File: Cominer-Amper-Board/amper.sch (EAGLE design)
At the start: 3 parts, among them U1 ESP-07

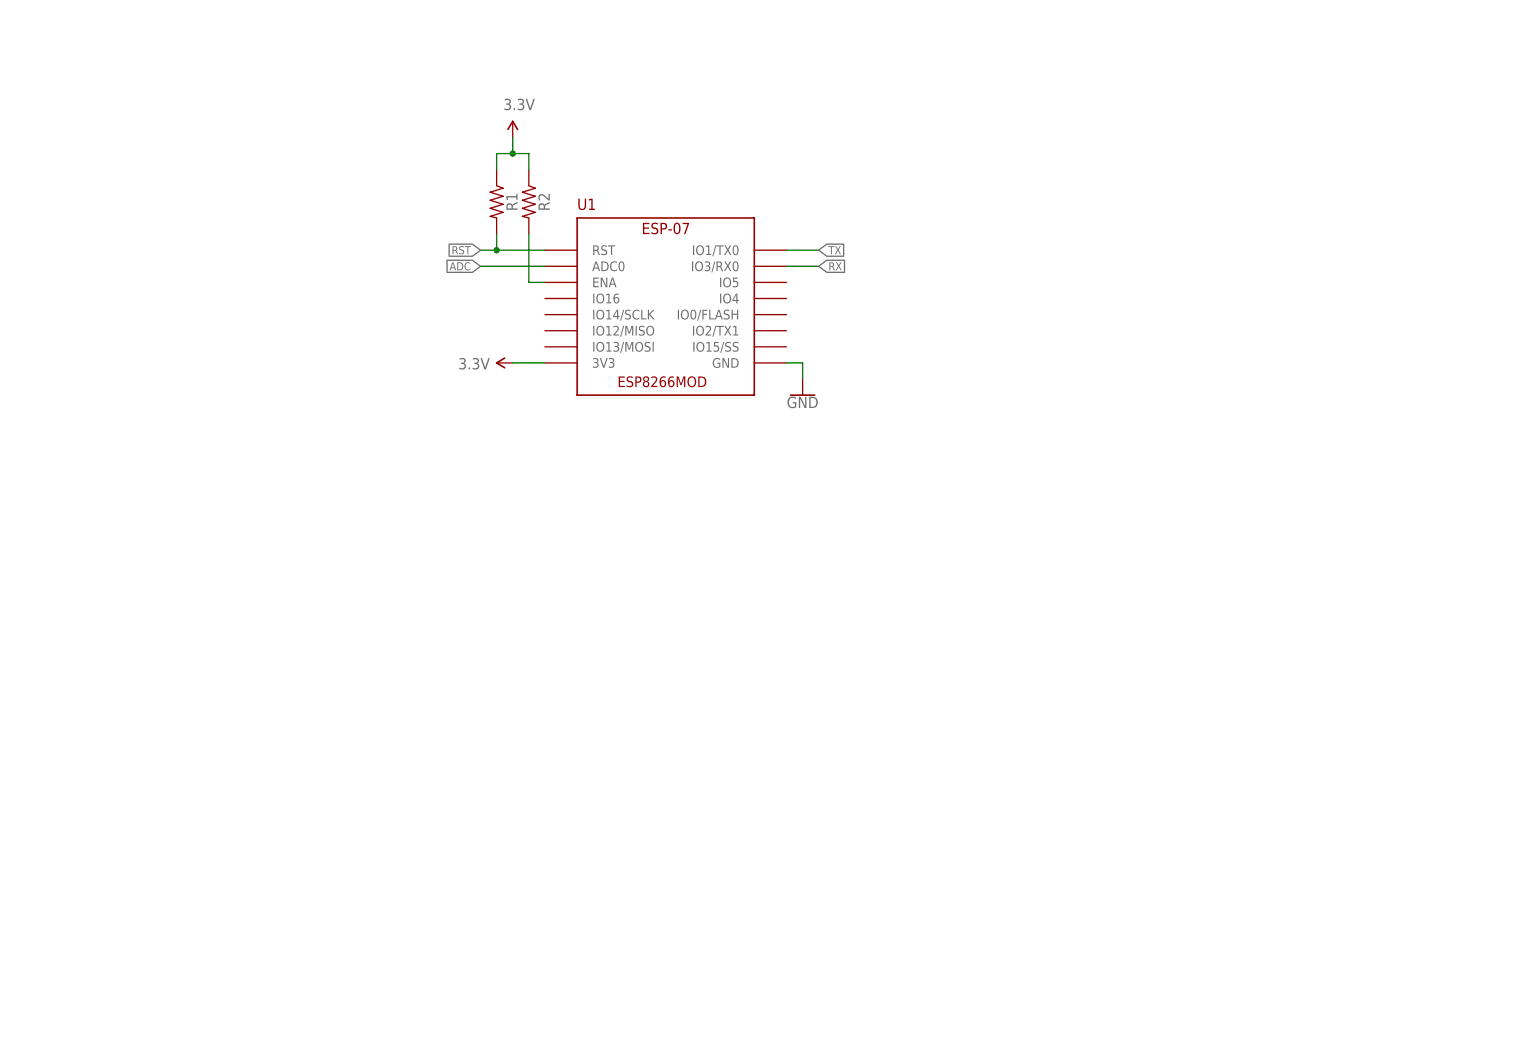
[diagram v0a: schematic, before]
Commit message: add usb to serialport circuit and lm1117 regulator
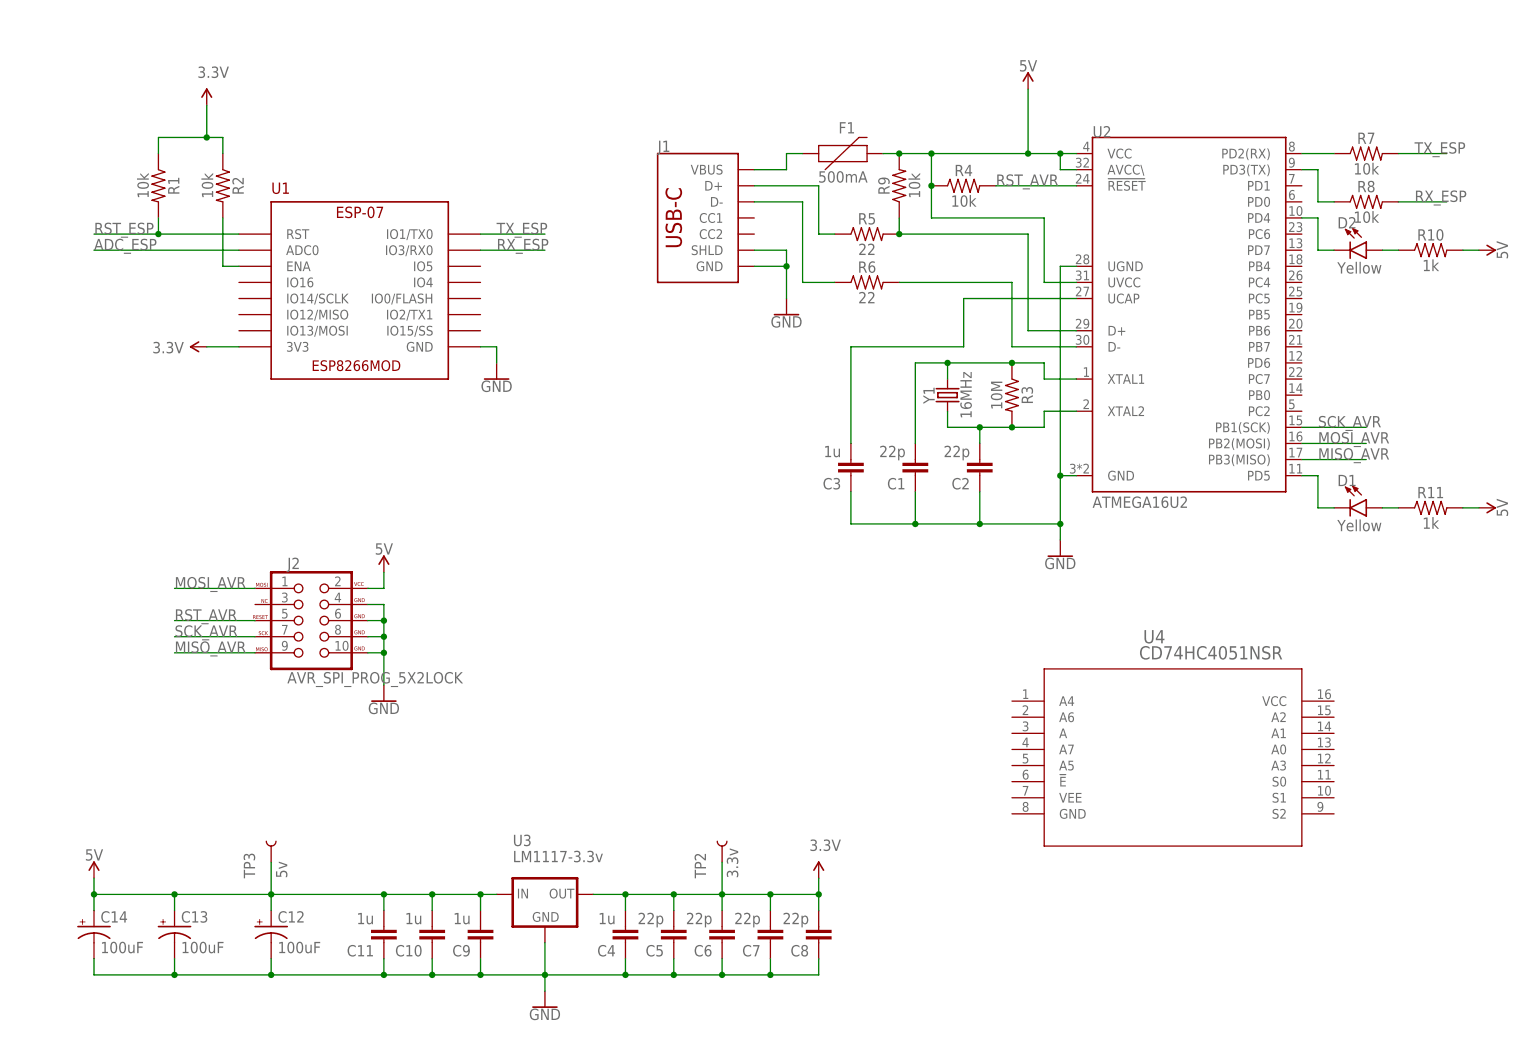
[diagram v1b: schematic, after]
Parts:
- added C1, C2, C5, C6, C7, C8: 22p, SparkFun-Capacitors:CAP-0805
- added C10, C11, C3, C4, C9: 1u, SparkFun-Capacitors:CAP-0805
- added C12, C13, C14: 100uF, SparkFun-Capacitors:100UF-POLAR-25V-20%(ELEC)
- added D1, D2: Yellow, SparkFun-LED:LED-YELLOW0603
- added F1: 500mA, SparkFun-Fuses:PPTC_16V_2.5A
- added J1: (no value), SparkFun-Connectors:USB_C_2-LAYER_PADS
- added J2: AVR_SPI_PROG_5X2LOCK, SparkFun-Connectors:AVR_SPI_PROG_5X2LOCK
- added R10, R11: 1k, SparkFun-Resistors:RESISTOR0805
- added R3: 10M, SparkFun-Resistors:RESISTOR0805
- added R4, R7, R8, R9: 10k, SparkFun-Resistors:RESISTOR0805
- added R5, R6: 22, SparkFun-Resistors:RESISTOR0805
- added TP2: 3.3v, SparkFun-Connectors:TEST-POINT3X4
- added TP3: 5v, SparkFun-Connectors:TEST-POINT3X4
- added U2: ATMEGA16U2, Cominer-Microcontroller:ATMEGA16U2
- added U3: LM1117-3.3v, SparkFun-IC-Power:V_REG_LD1117VXXLD1117-SMD
- added U4: CD74HC4051NSR, Cominer-CD74HC4051NSR:CD74HC4051NSR
- added Y1: 16MHz, SparkFun-Clocks:CRYSTAL-16MHZSMD-5X3.2
- R1, R2: value (none) -> 10k
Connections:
- net ADC renamed ADC_ESP
- net RST renamed RST_ESP
- removed net RX: U1.IO3/RX0
- removed net TX: U1.IO1/TX0
- new net 5V: C10.2, C11.2, C12.+, C13.+, C14.+, C9.2, F1.2, J2.VCC, R10.2, R11.2, R4.1, R9.2, TP3.1, U2.AVCC\, U2.UVCC, U2.VCC, U3.IN
- new net MISO_AVR: J2.MISO, U2.PB3(MISO)
- new net MOSI_AVR: J2.MOSI, U2.PB2(MOSI)
- new net N$1: C1.2, R3.1, U2.XTAL1, Y1.2
- new net N$10: F1.1, J1.VBUS
- new net N$11: R7.1, U2.PD2(RX)
- new net N$12: D1.C, U2.PD5
- new net N$13: D2.A, R10.1
- new net N$15: D1.A, R11.1
- new net N$2: C2.2, R3.2, U2.XTAL2, Y1.1
- new net N$3: C3.2, U2.UCAP
- new net N$4: D2.C, U2.PD4
- new net N$5: R8.1, U2.PD3(TX)
- new net N$6: R6.2, U2.D-
- new net N$7: R5.2, R9.1, U2.D+
- new net N$8: J1.D+, R5.1
- new net N$9: J1.D-, R6.1
- new net RST_AVR: J2.RESET, R4.2, U2.!RESET
- new net RX_ESP: R8.2, U1.IO3/RX0
- new net SCK_AVR: J2.SCK, U2.PB1(SCK)
- new net TX_ESP: R7.2, U1.IO1/TX0
- net 3.3V: now also C4.2, C5.2, C6.2, C7.2, C8.2, TP2.1, U3.OUT
- net GND: now also C1.1, C10.1, C11.1, C12.-, C13.-, C14.-, C2.1, C3.1, C4.1, C5.1, C6.1, C7.1, C8.1, C9.1, J1.GND, J1.SHLD, J2.GND@1, J2.GND@2, J2.GND@3, J2.GND@4, U2.GND, U2.UGND, U3.GND
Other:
- moved on the sheet: R1, R2, U1

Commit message: all devices were order
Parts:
- removed C10, C11, C9: 1u, SparkFun-Capacitors:CAP-0805
- removed C13, C14: 100uF, SparkFun-Capacitors:100UF-POLAR-25V-20%(ELEC)
- removed C7, C8: 22p, SparkFun-Capacitors:CAP-0805
- removed D1, D2: Yellow, SparkFun-LED:LED-YELLOW0603
- removed R10, R11: 1k, SparkFun-Resistors:RESISTOR0805
- removed R7, R8: 10k, SparkFun-Resistors:RESISTOR0805
- removed TP2: 3.3v, SparkFun-Connectors:TEST-POINT3X4
- removed TP3: 5v, SparkFun-Connectors:TEST-POINT3X4
- added C17, C18, C19: 0.1u, SparkFun-Capacitors:CAP-0805
- added C20: 1u, SparkFun-Capacitors:CAP-0805
- added C23: 100uF, SparkFun-Capacitors:100UF-POLAR-25V-20%(ELEC)
- added D3: STATUS, SparkFun-LED:LED-YELLOW0603
- added D4: ALARM, SparkFun-LED:LED-YELLOW0603
- added D5: POWER, SparkFun-LED:LED-YELLOW0603
- added IC1: OP-AMP, SparkFun-IC-Amplifiers:OPAMP-DUALU
- added J3, J4, J5, J6: AUDIO_JACK_3.5MM_PTH, SparkFun-Connectors:AUDIO_JACK_3.5MM_PTH
- added J7: MOLEX-CPU-POWER, Cominer-Connectors:MOLEX-CPU-POWER
- added J8: POWER_JACKSLT, SparkFun-Connectors:POWER_JACKSLT
- added Q1, Q2, Q3, Q4, Q5, Q6: 220mA/50V/3.5Ω, SparkFun-DiscreteSemi:MOSFET-NCH-BSS138
- added Q7: 20V/2A, SparkFun-DiscreteSemi:MOSFET_PCH-DMG2305UX-7
- added R12, R13, R14, R15, R16, R17, R18, R19, R20, R21, R22, R23, R24, R25: 10k, SparkFun-Resistors:RESISTOR0805
- added R26, R27, R28: 1k, SparkFun-Resistors:RESISTOR0805
- added U5, U6: ADS1015, SparkFun-IC-Conversion:ADS1015
- C4: value 1u -> 0.1u
- C5, C6: value 22p -> 0.1u
- U4: value CD74HC4051NSR -> LM1117-5v; device Cominer-CD74HC4051NSR:CD74HC4051NSR -> SparkFun-IC-Power:V_REG_LD1117VXXLD1117-SMD
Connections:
- removed net ADC_ESP: U1.ADC0
- removed net N$11: R7.1, U2.PD2(RX)
- removed net N$12: D1.C, U2.PD5
- removed net N$13: D2.A, R10.1
- removed net N$15: D1.A, R11.1
- removed net N$4: D2.C, U2.PD4
- removed net N$5: R8.1, U2.PD3(TX)
- new net N$16: J3.SLEEVE, U5.AIN0
- new net N$17: J3.TIP, U5.AIN1
- new net N$18: J4.TIP, U5.AIN3
- new net N$19: J4.SLEEVE, U5.AIN2
- new net N$20: J5.TIP, U6.AIN1
- new net N$21: Q1.D, R14.2, U5.SDA
- new net N$22: J5.SLEEVE, U6.AIN0
- new net N$23: Q2.D, R13.2, U5.SCL
- new net N$24: J6.TIP, U6.AIN3
- new net N$25: J6.SLEEVE, U6.AIN2
- new net N$26: Q3.D, R17.2, U6.SCL
- new net N$27: Q4.D, R18.2, U6.SDA
- new net N$28: IC1G1.OUT, Q7.G
- new net N$29: IC1G1.+IN, R24.1, R25.2
- new net N$30: D3.C, U1.IO16
- new net N$31: D4.C, U1.IO14/SCLK
- new net N$32: D3.A, R26.2
- new net N$33: D4.A, R27.2
- new net N$36: D5.A, R28.1
- new net RX_AVR: Q6.D, R22.2, U2.PD2(RX)
- new net SCL_ADC: Q2.S, Q3.S, R12.2, R16.2, U1.IO5
- new net SDA_ADC: Q1.S, Q4.S, R15.2, R19.2, U1.IO4
- new net TX_AVR: Q5.D, R21.2, U2.PD3(TX)
- new net USBVCC: F1.2, Q7.D, R9.2, U2.UVCC
- new net VIN: C12.+, C20.2, C23.+, J7.12VCD, J8.PWR, R24.2, U4.IN
- net 3.3V: now also IC1G1.-IN, Q1.G, Q2.G, Q3.G, Q4.G, Q5.G, Q6.G, R12.1, R15.1, R16.1, R19.1, R20.1, R23.1; no longer C7.2, C8.2, TP2.1
- net 5V: now also C17.2, C18.2, C19.2, IC1G3.P$V+, J3.TSH, J4.TSH, J5.TSH, J6.TSH, Q7.S, R13.1, R14.1, R17.1, R18.1, R21.1, R22.1, R26.1, R27.1, R28.2, U4.OUT, U5.ADDR, U5.VDD, U6.VDD; no longer C10.2, C11.2, C12.+, C13.+, C14.+, C9.2, F1.2, R10.2, R11.2, R9.2, TP3.1, U2.UVCC
- net GND: now also C17.1, C18.1, C19.1, C20.1, C23.-, D5.C, IC1G3.P$V-, J7.GND, J8.GND, J8.GNDBREAK, R25.1, U4.GND, U5.VSS, U6.ADDR, U6.VSS; no longer C10.1, C11.1, C13.-, C14.-, C7.1, C8.1, C9.1
- net N$1: now also Y1.1; no longer Y1.2
- net N$2: now also Y1.2; no longer Y1.1
- net RX_ESP: now also Q5.S, R20.2; no longer R8.2
- net TX_ESP: now also Q6.S, R23.2; no longer R7.2

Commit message: cominer-amp board complete
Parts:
- added C10, C11, C13, C7, C8, C9: 0.1u, SparkFun-Capacitors:CAP-0805
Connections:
- net 5V: now also C10.2, C11.2, C13.2, C7.2, C8.2, C9.2
- net GND: now also C10.1, C11.1, C13.1, C7.1, C8.1, C9.1
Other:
- moved on the sheet: C12, C17, C18, C19, C20, C23, C4, C5, C6, U3, U4
